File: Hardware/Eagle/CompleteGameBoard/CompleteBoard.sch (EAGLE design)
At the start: 21 parts

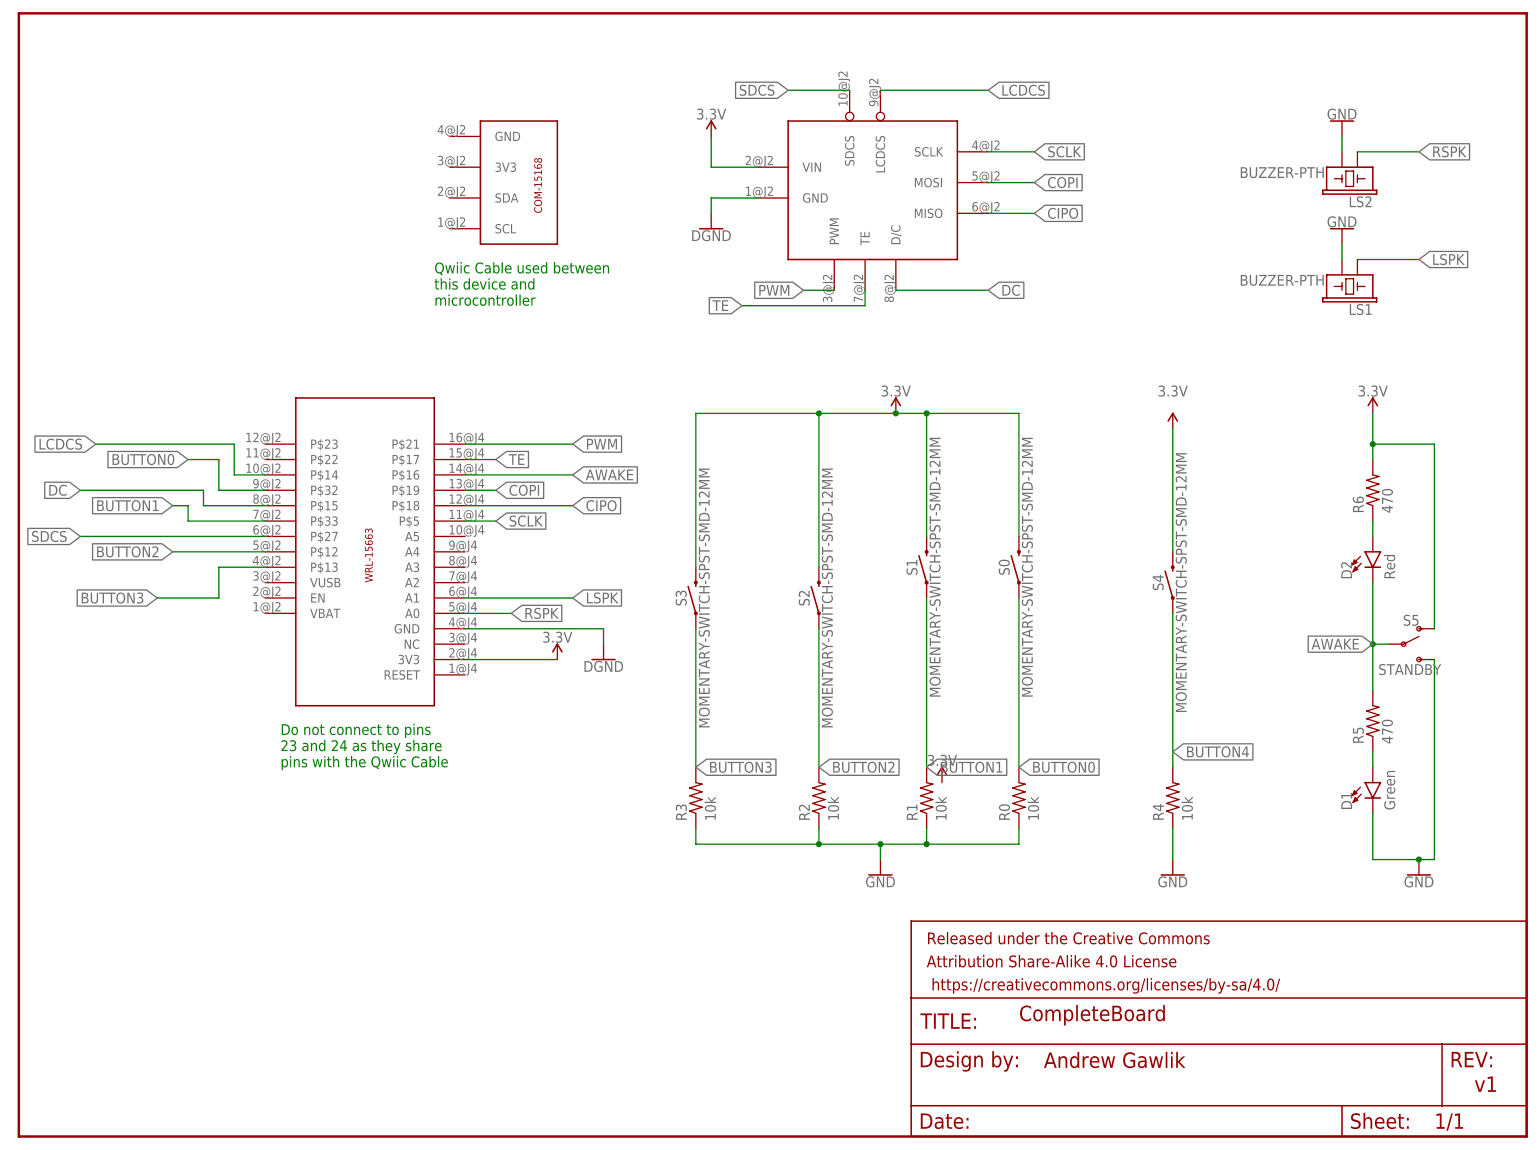
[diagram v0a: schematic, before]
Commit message: Updated Wiring and parts for issue #12 so that through hole buttons are used
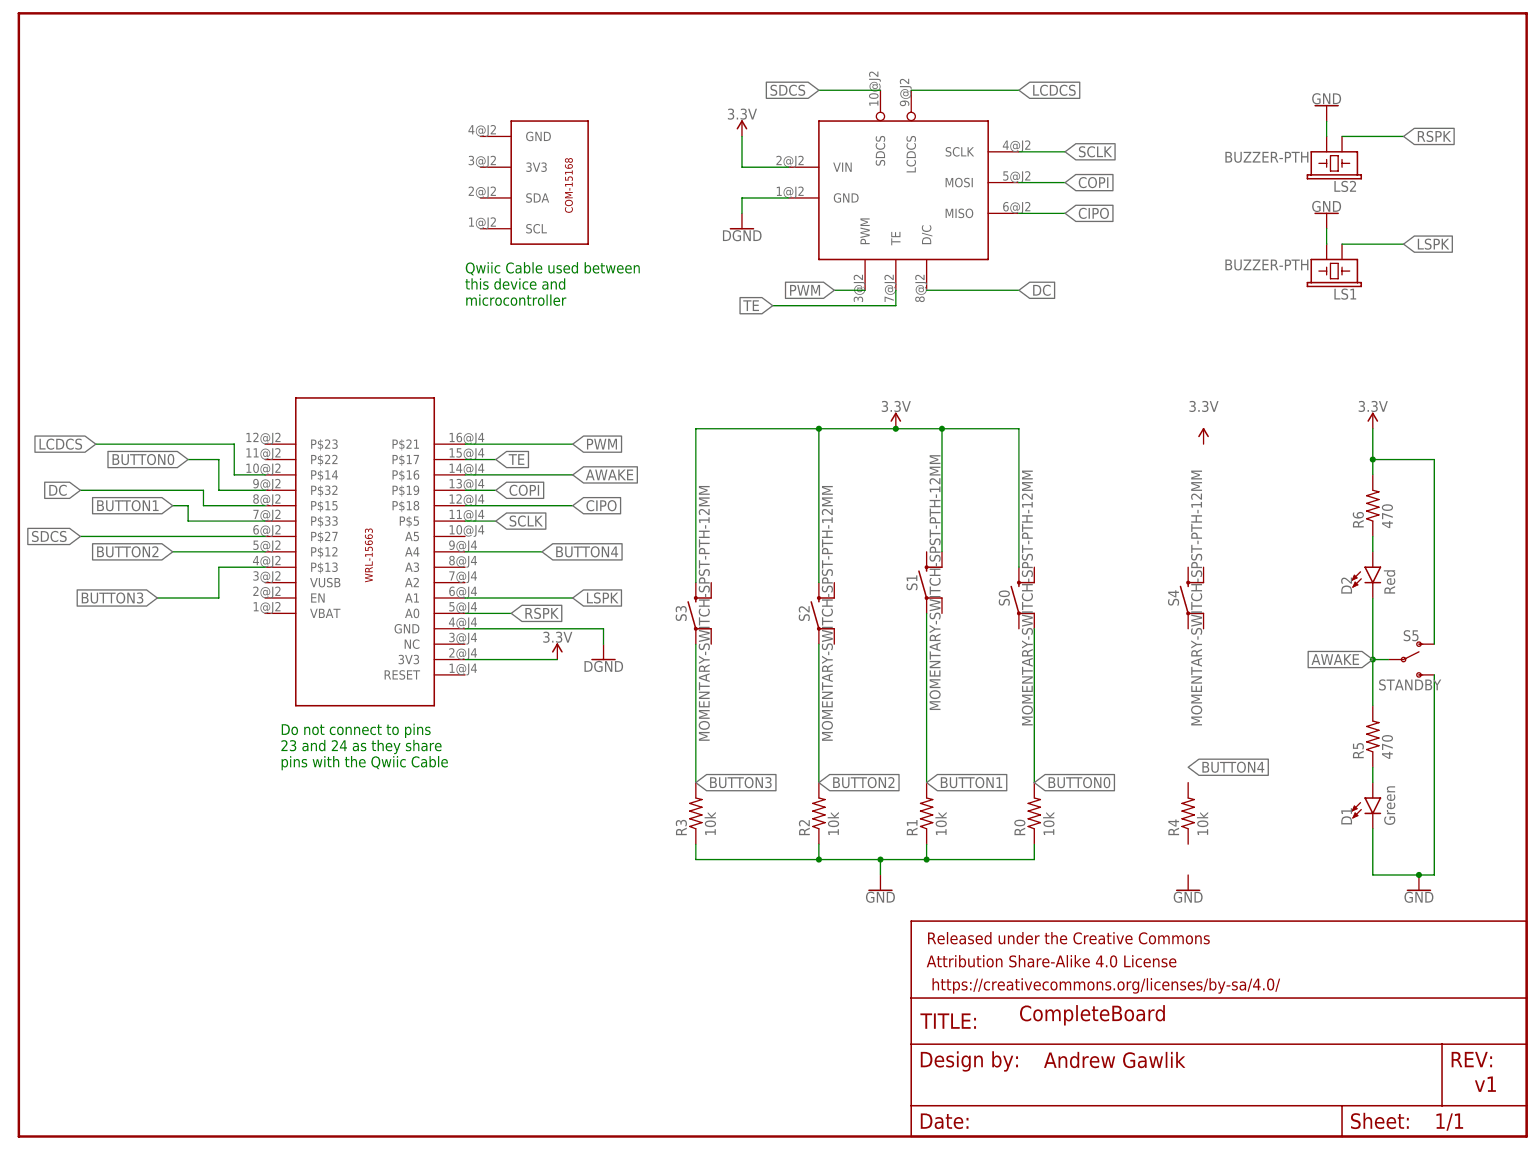
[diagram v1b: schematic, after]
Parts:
- S0, S1, S2, S3, S4: value MOMENTARY-SWITCH-SPST-SMD-12MM -> MOMENTARY-SWITCH-SPST-PTH-12MM; device SparkFun-Switches:MOMENTARY-SWITCH-SPST-SMD-12MM -> SparkFun-Switches:MOMENTARY-SWITCH-SPST-PTH-12MM
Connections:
- net 3.3V: now also S0.3, S1.4, S2.3, S3.3; no longer S0.2, S1.2, S2.2, S3.2, S4.2
- net BUTTON0: now also S0.2; no longer S0.1
- net BUTTON4: now also A1.A4; no longer R4.2, S4.1
- net GND: no longer R4.1
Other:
- moved on the sheet: D1, D2, LS1, LS2, R0, R1, R2, R3, R4, R5, R6, S5
